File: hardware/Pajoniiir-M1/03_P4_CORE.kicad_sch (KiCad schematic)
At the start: 42 parts, among them U1 ESP32-P4NRW32X, U3 TLV62569DRLR

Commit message: hardware: fix local symbol cache keys for ERC
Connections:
- net 3V3_SYS: now also U1.101 (VDD_ANA)
- net BOOT_GPIO35: now also U1.43 (CSI_DATAP0)
- net BOOT_GPIO36: now also U1.42 (CSI_DATAN0)
- net C6_SDIO_CLK: now also U1.5 (GPIO5)
- net C6_SDIO_CMD: now also U1.4 (GPIO4)
- net C6_SDIO_D0: now also U1.10 (GPIO9)
- net C6_SDIO_D1: now also U1.8 (GPIO8)
- net C6_SDIO_D2: now also U1.7 (GPIO7)
- net C6_SDIO_D3: now also U1.6 (GPIO6)
- net CHIP_PU: now also U1.78 (FB_DCDC)
- net I2C_SCL: now also U1.16 (GPIO15)
- net I2C_SDA: now also U1.17 (GPIO16/ADC1_CHANNEL0)
- net LCD_BL_PWM: now also U1.104 (GPIO0)
- net LCD_RST: now also U1.19 (GPIO18/ADC1_CHANNEL2)
- net LCD_TE: now also U1.18 (GPIO17/ADC1_CHANNEL1)
- net P4_EN_DCDC: now also U1.100 (XTAL_P)
- net P4_FB_DCDC: now also U1.103 (CHIP_PU)
- net P4_USBJTAG_DM: now also U1.53 (GPIO25/USB1P1_P0)
- net P4_USBJTAG_DP: now also U1.52 (GPIO24/USB1P1_N0)
- net P4_VDDO_PSRAM: now also U1.59 (VDD_PSRAM_0), U1.72 (VDDO_PSRAM)
- net P4_VDD_ANA: now also U1.85 (VDD_IO_5)
- net TOUCH_INT: now also U1.20 (GPIO19/ADC1_CHANNEL3)
- net TOUCH_RST: now also U1.22 (GPIO20/ADC1_CHANNEL4)
- net USB0_FAULT_N: now also U1.2 (GPIO2)
- net USB0_HS_DM: now also U1.57 (GPIO28)
- net USB0_HS_DP: now also U1.56 (GPIO27/USB1P1_P1)
- net USB0_PWR_EN: now also U1.3 (GPIO3)
- net USB1_FAULT_N: now also U1.46 (CSI_DATAN1)
- net USB1_FS_DP: now also U1.50 (USB-DP)
- net USB1_PWR_EN: now also U1.1 (GPIO1)
- net XTAL_P: now also U1.79 (EN_DCDC)

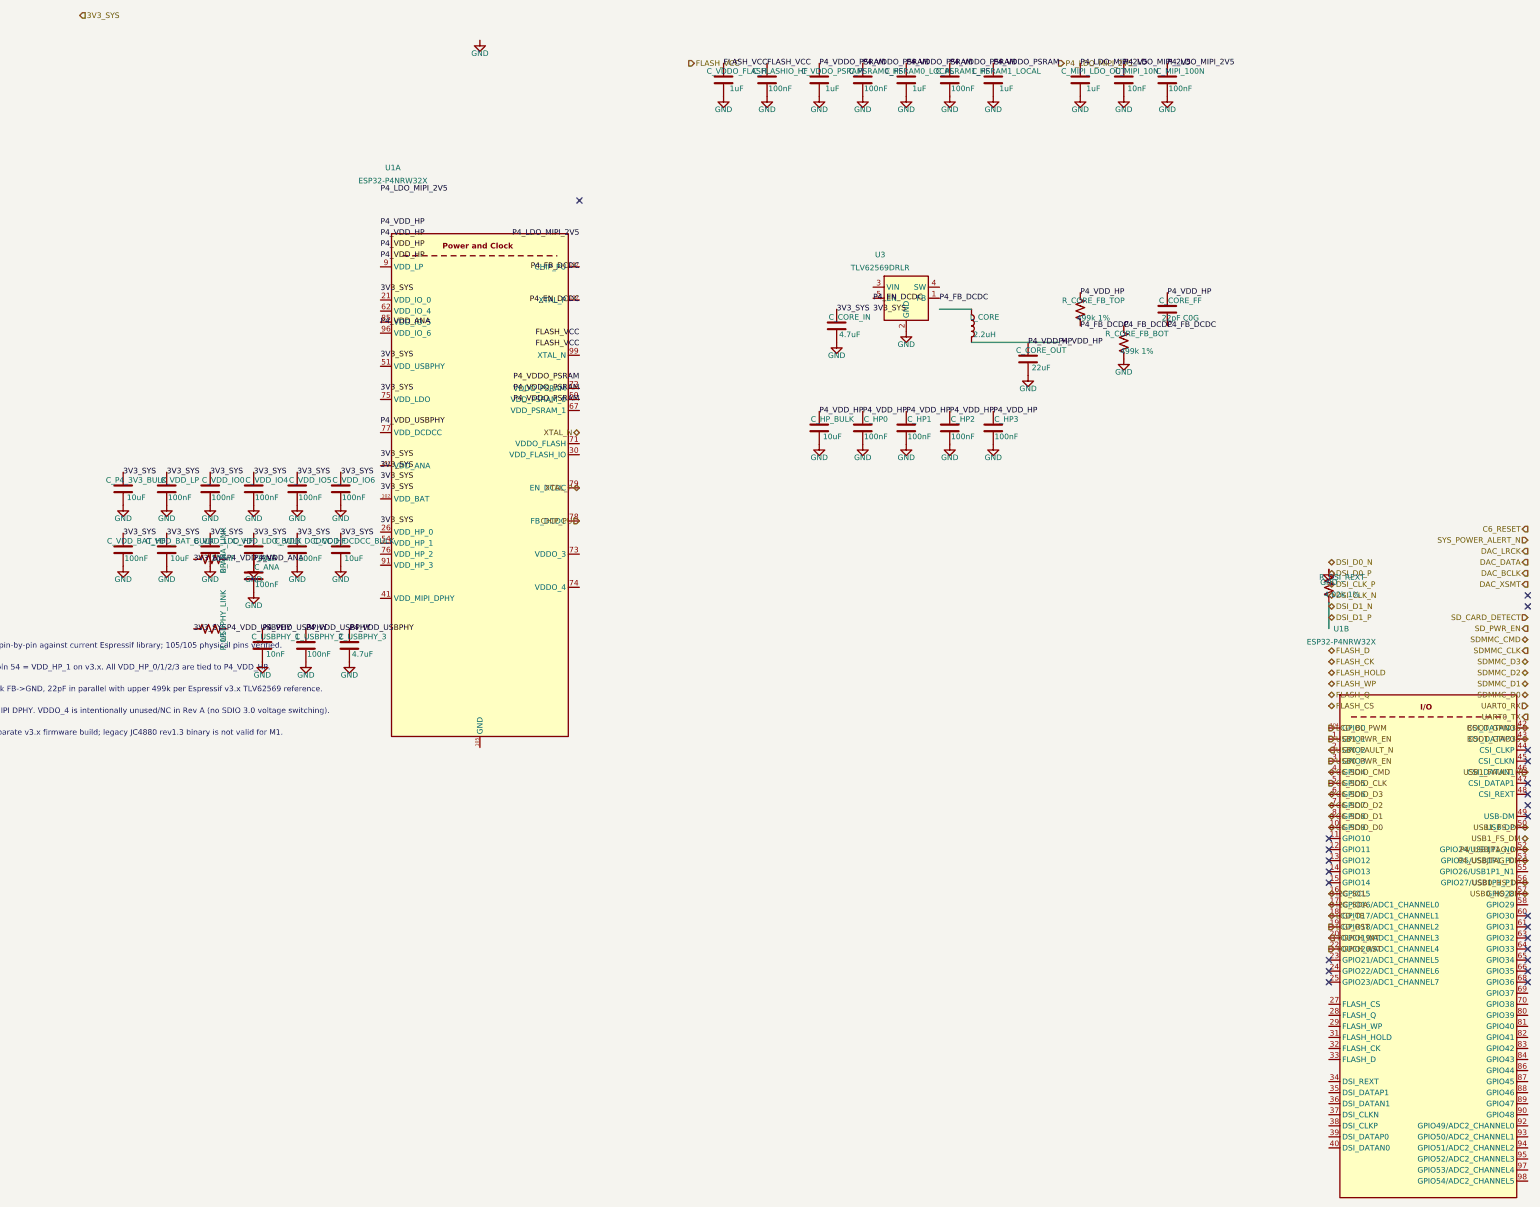
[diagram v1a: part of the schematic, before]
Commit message: hardware: snap child sheets 01-05 to 25 mil grid
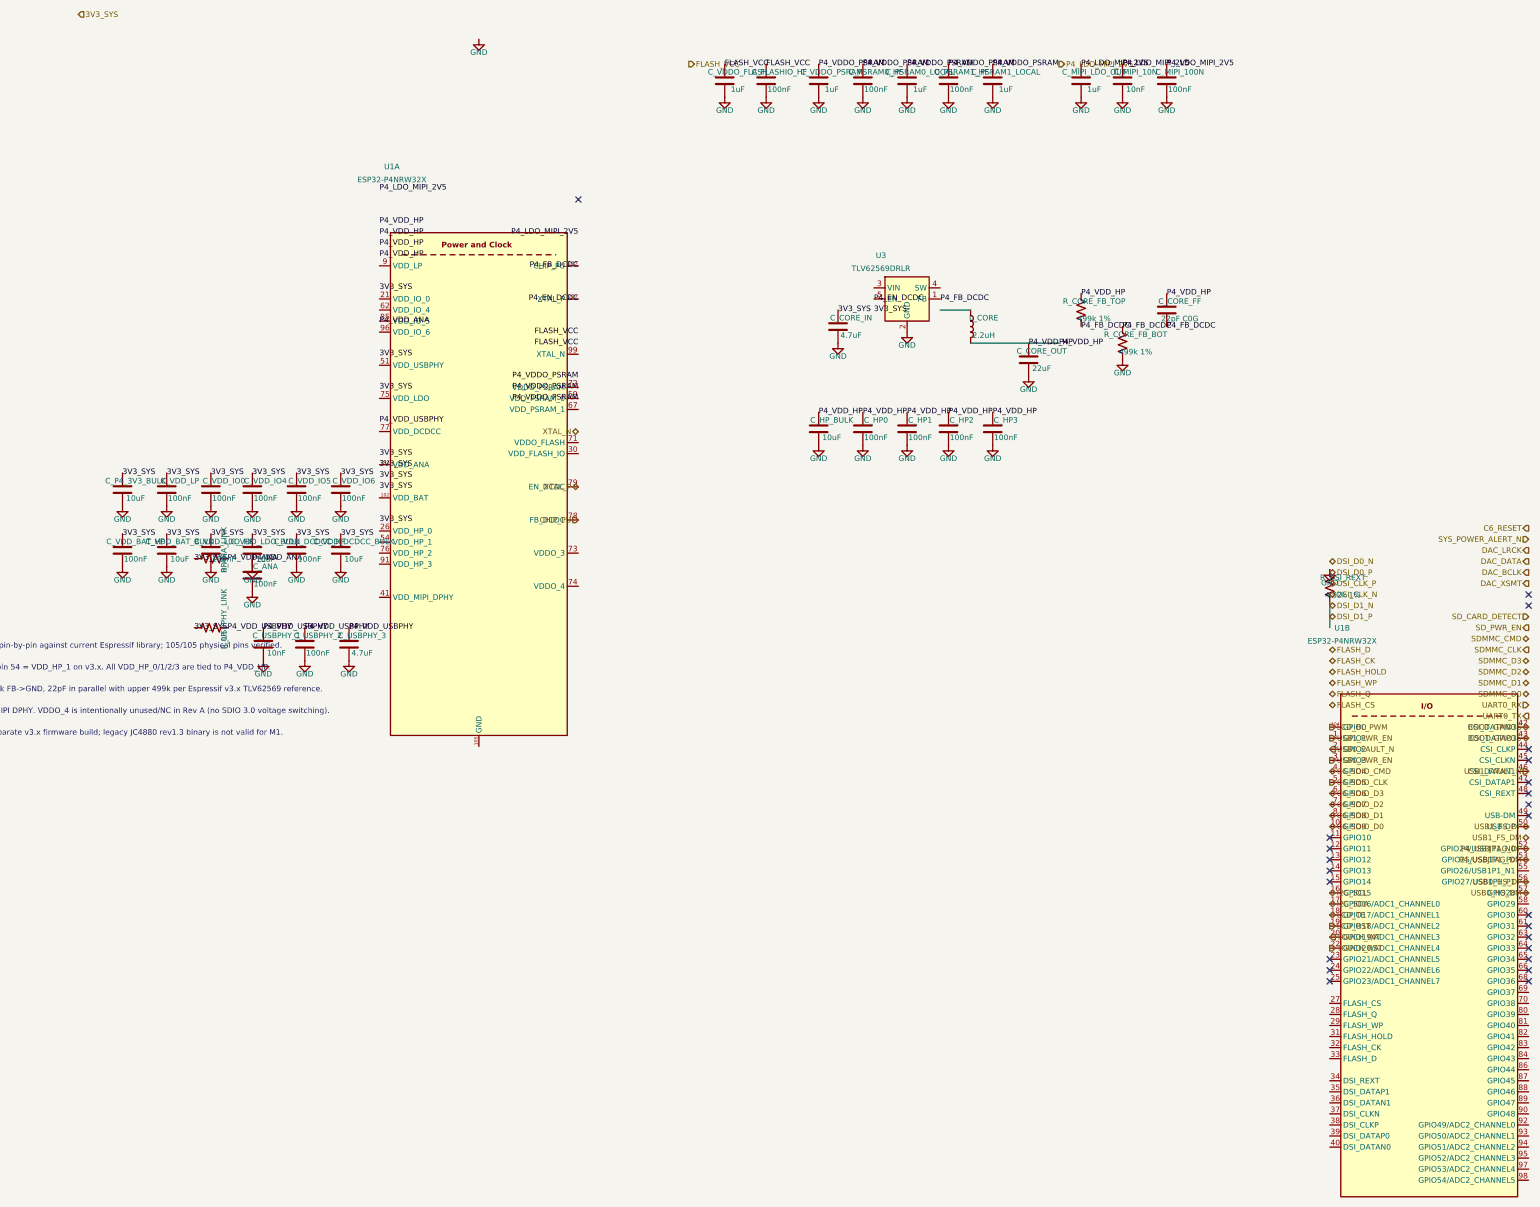
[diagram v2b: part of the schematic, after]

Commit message: hardware: bind core hierarchical ports to nets
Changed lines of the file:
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@@
     (instances (project "Pajoniiir-M1" (path "/2c8dd352-b7b8-4d9e-8f93-5dd43be2a100/31000003-6b2a-4a3a-8c91-000000000003" (reference "#PWR0301") (unit 1))))
   )
-  (label "3V3_SYS" (at 88.9 140.97 0) (effects (font (size 1.27 1.27))))
   (label "3V3_SYS" (at 88.9 133.35 0) (effects (font (size 1.27 1.27))))
   (label "3V3_SYS" (at 88.9 130.81 0) (effects (font (size 1.27 1.27))))
@@
     (instances (project "Pajoniiir-M1" (path "/2c8dd352-b7b8-4d9e-8f93-5dd43be2a100/31000003-6b2a-4a3a-8c91-000000000003" (reference "#PWR0392") (unit 1))))
   )
-  (label "FLASH_VCC" (at 134.62 100.33 180) (effects (font (size 1.27 1.27))))
   (label "FLASH_VCC" (at 134.62 97.79 180) (effects (font (size 1.27 1.27))))
-  (hierarchical_label "FLASH_VCC" (shape output) (at 160.02 36.195 0) (effects (font (size 1.27 1.27))))
+  (hierarchical_label "FLASH_VCC" (shape output) (at 134.62 100.33 180) (effects (font (size 1.27 1.27))))
   (symbol
     (lib_id "Device:C") (at 168.275 40.005 0) (unit 1)
@@
     (instances (project "Pajoniiir-M1" (path "/2c8dd352-b7b8-4d9e-8f93-5dd43be2a100/31000003-6b2a-4a3a-8c91-000000000003" (reference "#PWR033230") (unit 1))))
   )
-  (label "P4_LDO_MIPI_2V5" (at 134.62 74.93 180) (effects (font (size 1.27 1.27))))
   (label "P4_LDO_MIPI_2V5" (at 88.9 64.77 0) (effects (font (size 1.27 1.27))))
-  (hierarchical_label "P4_LDO_MIPI_2V5" (shape output) (at 245.11 36.195 0) (effects (font (size 1.27 1.27))))
+  (hierarchical_label "P4_LDO_MIPI_2V5" (shape output) (at 134.62 74.93 180) (effects (font (size 1.27 1.27))))
   (symbol
     (lib_id "Device:C") (at 250.19 40.005 0) (unit 1)
@@
     (instances (project "Pajoniiir-M1" (path "/2c8dd352-b7b8-4d9e-8f93-5dd43be2a100/31000003-6b2a-4a3a-8c91-000000000003" (reference "#PWR03780") (unit 1))))
   )
-  (hierarchical_label "3V3_SYS" (shape input) (at 19.685 24.765 0) (effects (font (size 1.27 1.27))))
+  (hierarchical_label "3V3_SYS" (shape input) (at 88.9 140.97 0) (effects (font (size 1.27 1.27))))
   (no_connect (at 307.34 247.015))
   (no_connect (at 307.34 224.155))
